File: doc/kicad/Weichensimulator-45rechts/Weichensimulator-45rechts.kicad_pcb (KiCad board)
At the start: 2 copper layers, 38.1 x 38.1 mm, 9 parts, among them J1 Conn_01x02_Male, J2 Power, J3 Conn_01x02_Male, K1 HFD2_005-S-L2-D

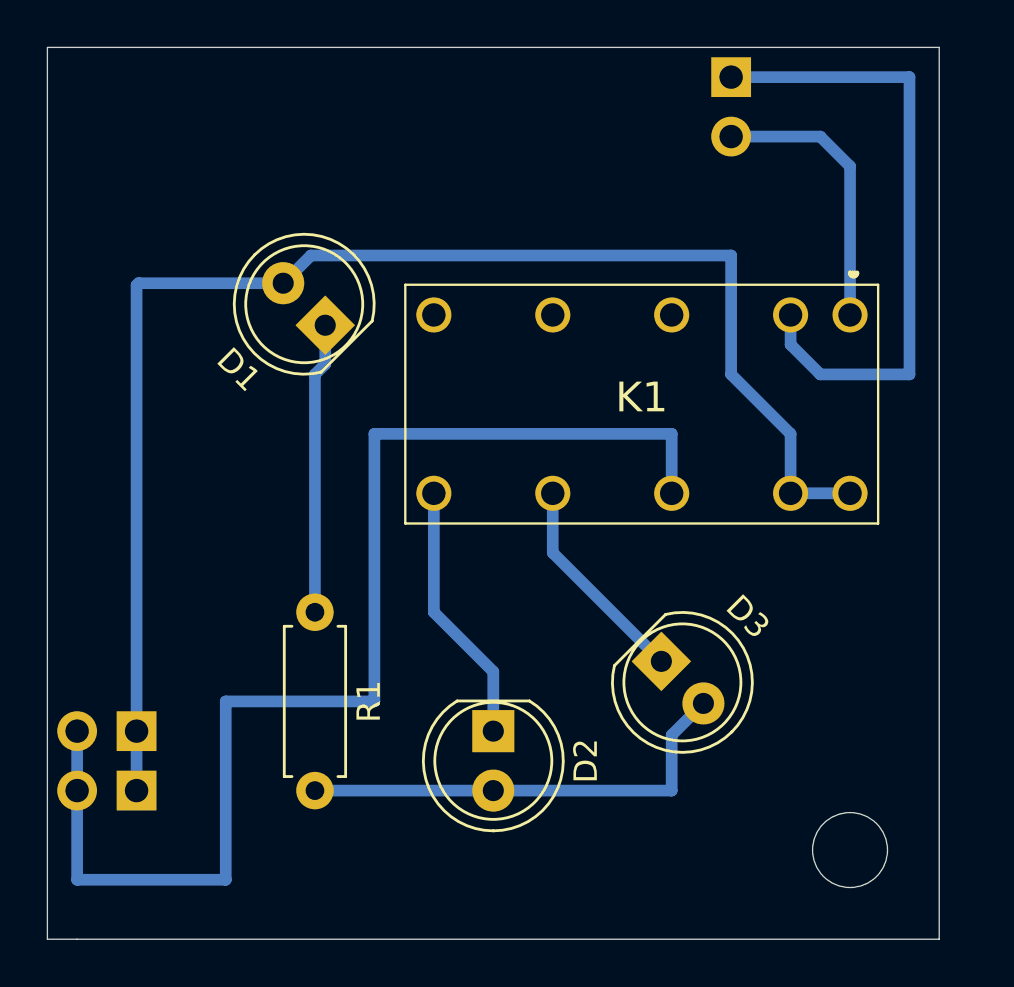
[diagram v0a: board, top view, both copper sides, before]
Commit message: Ecken rund gemacht, alle mit Montagelöcher
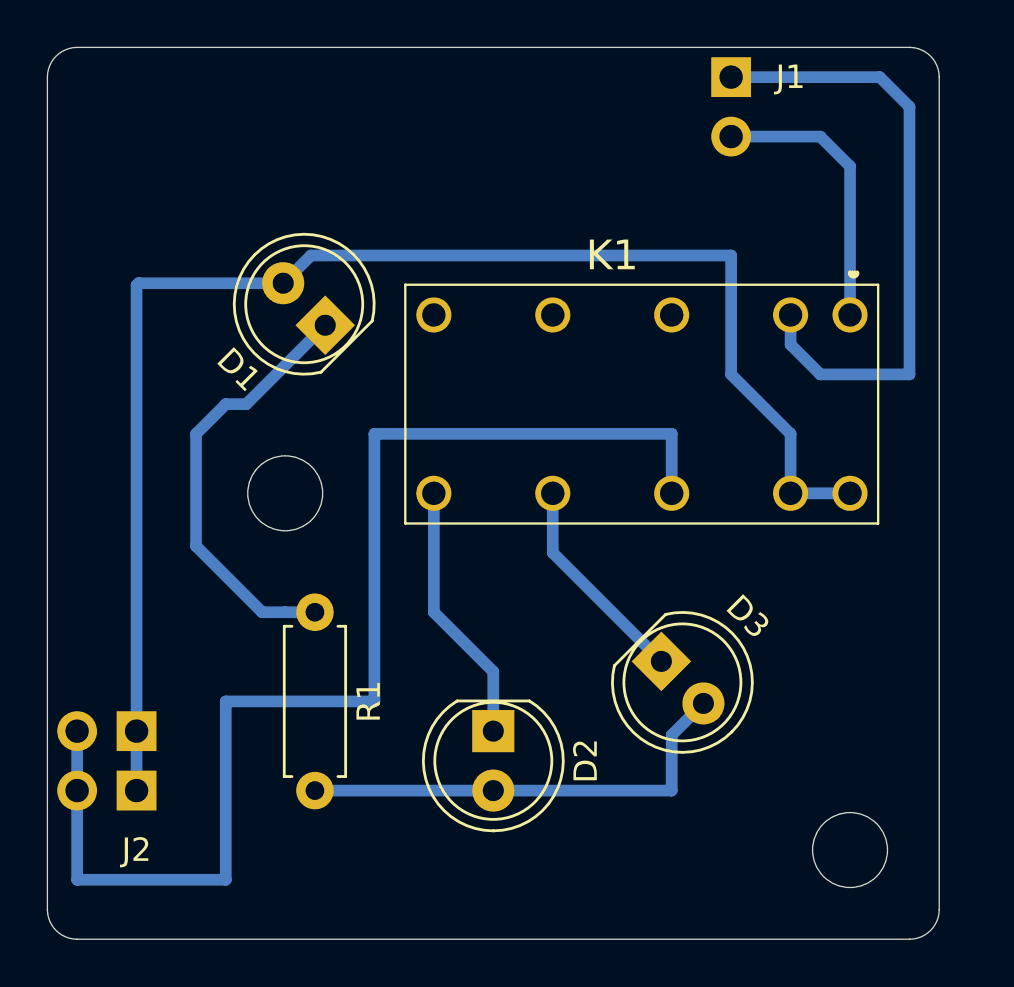
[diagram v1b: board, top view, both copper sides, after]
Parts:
- added H1: MountingHole, Mounting_Holes:MountingHole_3.2mm_M3, F.Cu at (139.7, 115.6)
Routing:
- net Net-(D1-Pad1): track 12.4 -> 18.5 mm
- net Net-(J1-Pad1): track 27.2 -> 26.5 mm
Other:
- outline, holes or cut-outs redrawn
- board text added: "©H3-H5N6 2021 Weiche re/45° v1.0"
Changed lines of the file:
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@@
-(kicad_pcb (version 20171130) (host pcbnew 5.1.9)
+(kicad_pcb (version 20171130) (host pcbnew 5.1.10)
   (general
     (thickness 1.6)
-    (drawings 5)
-    (tracks 38)
+    (drawings 9)
+    (tracks 43)
     (zones 0)
-    (modules 9)
+    (modules 10)
     (nets 9)
   )
@@
     (34 B.Paste user hide)
     (35 F.Paste user hide)
-    (36 B.SilkS user hide)
+    (36 B.SilkS user)
     (37 F.SilkS user)
     (38 B.Mask user)
@@
     (45 Margin user hide)
     (46 B.CrtYd user)
-    (47 F.CrtYd user hide)
+    (47 F.CrtYd user)
     (48 B.Fab user hide)
     (49 F.Fab user hide)
@@
     (add_net "Net-(J1-Pad2)")
   )
+  (module Mounting_Holes:MountingHole_3.2mm_M3 (layer F.Cu)
+    (at 139.7 115.57 270)
+    (descr "Mounting Hole 3.2mm, no annular, M3")
+    (tags "mounting hole 3.2mm no annular m3")
+    (attr virtual)
+    (fp_text reference H1 (at 0 -4.2 90) (layer F.SilkS) hide
+      (effects (font (size 1 1) (thickness 0.15)))
+    )
+    (fp_text value MountingHole (at 0 4.2 90) (layer F.Fab)
+      (effects (font (size 1 1) (thickness 0.15)))
+    )
+    (fp_text user %R (at 0.3 0 90) (layer F.Fab)
+      (effects (font (size 1 1) (thickness 0.15)))
+    )
+    (fp_circle (center 0 0) (end 3.2 0) (layer Cmts.User) (width 0.15))
+    (fp_circle (center 0 0) (end 3.45 0) (layer F.CrtYd) (width 0.05))
+    (pad "" np_thru_hole circle (at 0 0 270) (size 3.2 3.2) (drill 3.2) (layers *.Cu *.Mask)
+      (thermal_gap 2))
+  )
   (module LEDs:LED_D5.0mm (layer F.Cu)
     (at 141.41 108.39 135)
@@
     (descr HFD2/005-S-L2-D-3)
     (tags "Relay or Contactor")
-    (fp_text reference K1 (at 8.9 -3.53) (layer F.SilkS)
+    (fp_text reference K1 (at 10.16 2.54) (layer F.SilkS)
       (effects (font (size 1.27 1.27) (thickness 0.254)))
     )
@@
     (descr "Through hole angled pin header, 1x02, 2.54mm pitch, 6mm pin length, single row")
     (tags "Through hole angled pin header THT 1x02 2.54mm single row")
-    (fp_text reference J1 (at 4.385 2.27 180) (layer B.SilkS)
-      (effects (font (size 1 1) (thickness 0.15)) (justify mirror))
+    (fp_text reference J1 (at -2.54 0 180) (layer F.SilkS)
+      (effects (font (size 1 1) (thickness 0.15)))
     )
     (fp_text value Conn_01x02_Male (at 4.385 -4.81 180) (layer B.Fab)
@@
     (descr "Through hole angled pin header, 1x02, 2.54mm pitch, 6mm pin length, single row")
     (tags "Through hole angled pin header THT 1x02 2.54mm single row")
-    (fp_text reference J2 (at 4.385 2.27 90) (layer B.SilkS)
-      (effects (font (size 1 1) (thickness 0.15)) (justify mirror))
+    (fp_text reference J2 (at -5.08 0 180) (layer F.SilkS)
+      (effects (font (size 1 1) (thickness 0.15)))
     )
     (fp_text value Power (at 4.385 -4.81 90) (layer B.Fab)
@@
     (descr "Through hole angled pin header, 1x02, 2.54mm pitch, 6mm pin length, single row")
     (tags "Through hole angled pin header THT 1x02 2.54mm single row")
-    (fp_text reference J3 (at 4.385 2.27 90) (layer B.SilkS)
-      (effects (font (size 1 1) (thickness 0.15)) (justify mirror))
+    (fp_text reference J3 (at -2.54 0 180) (layer F.SilkS) hide
+      (effects (font (size 1 1) (thickness 0.15)))
     )
     (fp_text value Conn_01x02_Male (at 4.385 -4.81 90) (layer B.Fab)
@@
       (thermal_gap 2))
   )
-  (gr_line (start 129.54 134.62) (end 130.81 134.62) (layer Edge.Cuts) (width 0.05))
-  (gr_line (start 129.54 96.52) (end 167.64 96.52) (layer Edge.Cuts) (width 0.05))
-  (gr_line (start 129.54 134.62) (end 129.54 96.52) (layer Edge.Cuts) (width 0.05))
-  (gr_line (start 167.64 134.62) (end 130.81 134.62) (layer Edge.Cuts) (width 0.05))
-  (gr_line (start 167.64 96.52) (end 167.64 134.62) (layer Edge.Cuts) (width 0.05))
-  (segment (start 141.41 108.39) (end 141.41 110.05) (width 0.5) (layer B.Cu) (net 1))
-  (segment (start 141.41 110.05) (end 140.97 110.49) (width 0.5) (layer B.Cu) (net 1))
-  (segment (start 140.97 110.49) (end 140.97 120.65) (width 0.5) (layer B.Cu) (net 1))
+  (gr_text "©H3-H5N6 2021\nWeiche re/45° v1.0" (at 154.94 111.76) (layer B.SilkS)
+    (effects (font (size 1.5 1.5) (thickness 0.3)) (justify mirror))
+  )
+  (gr_arc (start 130.81 133.35) (end 129.54 133.35) (angle -90) (layer Edge.Cuts) (width 0.05))
+  (gr_arc (start 166.37 133.35) (end 166.37 134.62) (angle -90) (layer Edge.Cuts) (width 0.05))
+  (gr_arc (start 166.37 97.79) (end 167.64 97.79) (angle -90) (layer Edge.Cuts) (width 0.05))
+  (gr_arc (start 130.81 97.79) (end 130.81 96.52) (angle -90) (layer Edge.Cuts) (width 0.05))
+  (gr_line (start 130.81 96.52) (end 166.37 96.52) (layer Edge.Cuts) (width 0.05))
+  (gr_line (start 129.54 133.35) (end 129.54 97.79) (layer Edge.Cuts) (width 0.05))
+  (gr_line (start 166.37 134.62) (end 130.81 134.62) (layer Edge.Cuts) (width 0.05))
+  (gr_line (start 167.64 97.79) (end 167.64 133.35) (layer Edge.Cuts) (width 0.05))
+  (segment (start 139.7 120.65) (end 140.97 120.65) (width 0.5) (layer B.Cu) (net 1))
+  (segment (start 135.89 117.824001) (end 138.715999 120.65) (width 0.5) (layer B.Cu) (net 1))
+  (segment (start 138.715999 120.65) (end 139.7 120.65) (width 0.5) (layer B.Cu) (net 1))
+  (segment (start 135.89 113.03) (end 135.89 117.824001) (width 0.5) (layer B.Cu) (net 1))
+  (segment (start 137.16 111.76) (end 135.89 113.03) (width 0.5) (layer B.Cu) (net 1))
+  (segment (start 138.04 111.76) (end 137.16 111.76) (width 0.5) (layer B.Cu) (net 1))
+  (segment (start 141.41 108.39) (end 138.04 111.76) (width 0.5) (layer B.Cu) (net 1))
   (segment (start 146.05 115.57) (end 146.05 120.65) (width 0.5) (layer B.Cu) (net 2))
   (segment (start 146.05 120.65) (end 148.59 123.19) (width 0.5) (layer B.Cu) (net 2))
@@
   (segment (start 161.29 109.22) (end 162.56 110.49) (width 0.5) (layer B.Cu) (net 5))
   (segment (start 162.56 110.49) (end 166.37 110.49) (width 0.5) (layer B.Cu) (net 5))
-  (segment (start 166.37 110.49) (end 166.37 97.79) (width 0.5) (layer B.Cu) (net 5))
-  (segment (start 166.37 97.79) (end 158.75 97.79) (width 0.5) (layer B.Cu) (net 5))
+  (segment (start 166.37 99.06) (end 165.1 97.79) (width 0.5) (layer B.Cu) (net 5))
+  (segment (start 165.1 97.79) (end 158.75 97.79) (width 0.5) (layer B.Cu) (net 5))
+  (segment (start 166.37 99.06) (end 166.37 110.49) (width 0.5) (layer B.Cu) (net 5))
   (segment (start 133.35 125.73) (end 133.35 128.27) (width 0.5) (layer B.Cu) (net 6))
   (segment (start 139.613949 106.593949) (end 133.436051 106.593949) (width 0.5) (layer B.Cu) (net 6))

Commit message: Platinen, die an jlcpcb geschickt worden sind.
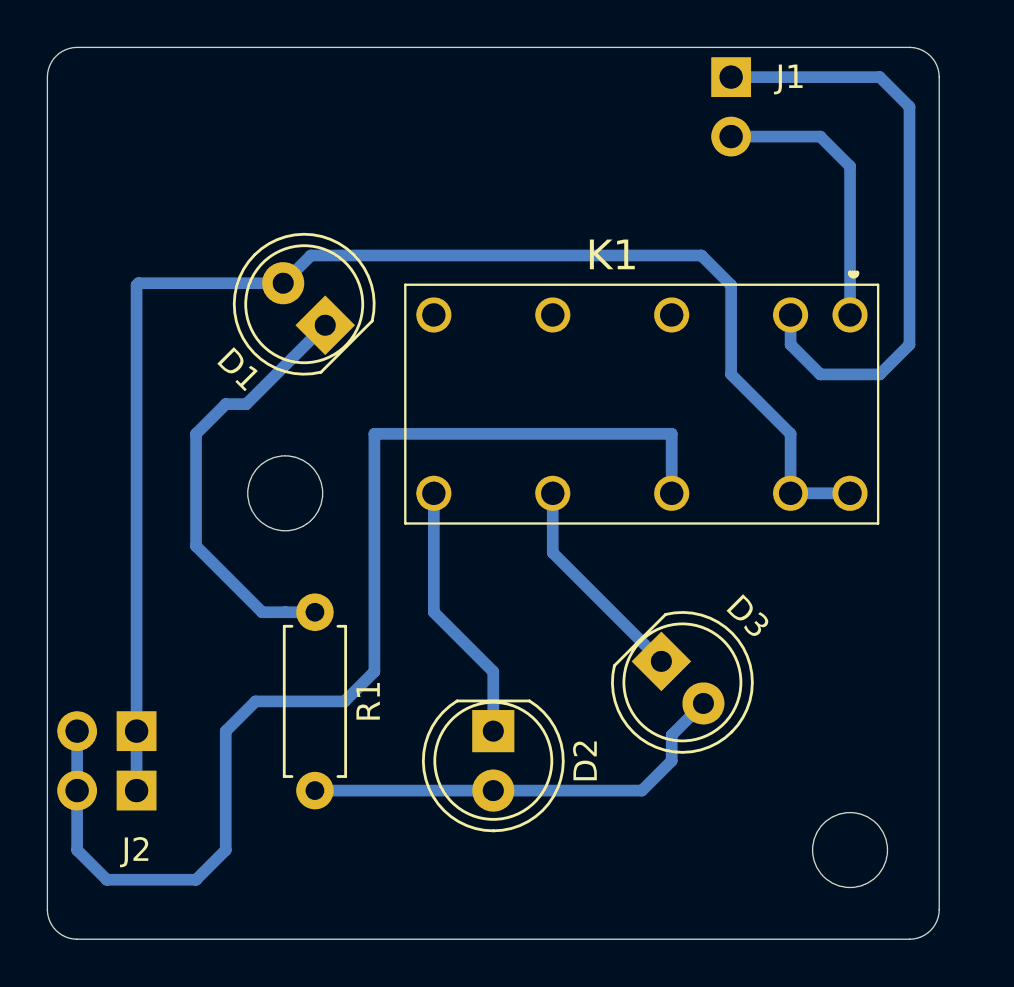
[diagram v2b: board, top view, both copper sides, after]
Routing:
- net GND: track 53.3 -> 50.4 mm
- net Net-(J1-Pad1): track 26.5 -> 25.7 mm
- net Net-(D2-Pad2): track 19.5 -> 18.8 mm
- net +5V: track 61.3 -> 60.5 mm
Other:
- board text added: "+5V"
- board text added: "A"
- board text added: "G"
- board text added: "GND"

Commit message: Bezeichnung nun auf der Besrückungsseite
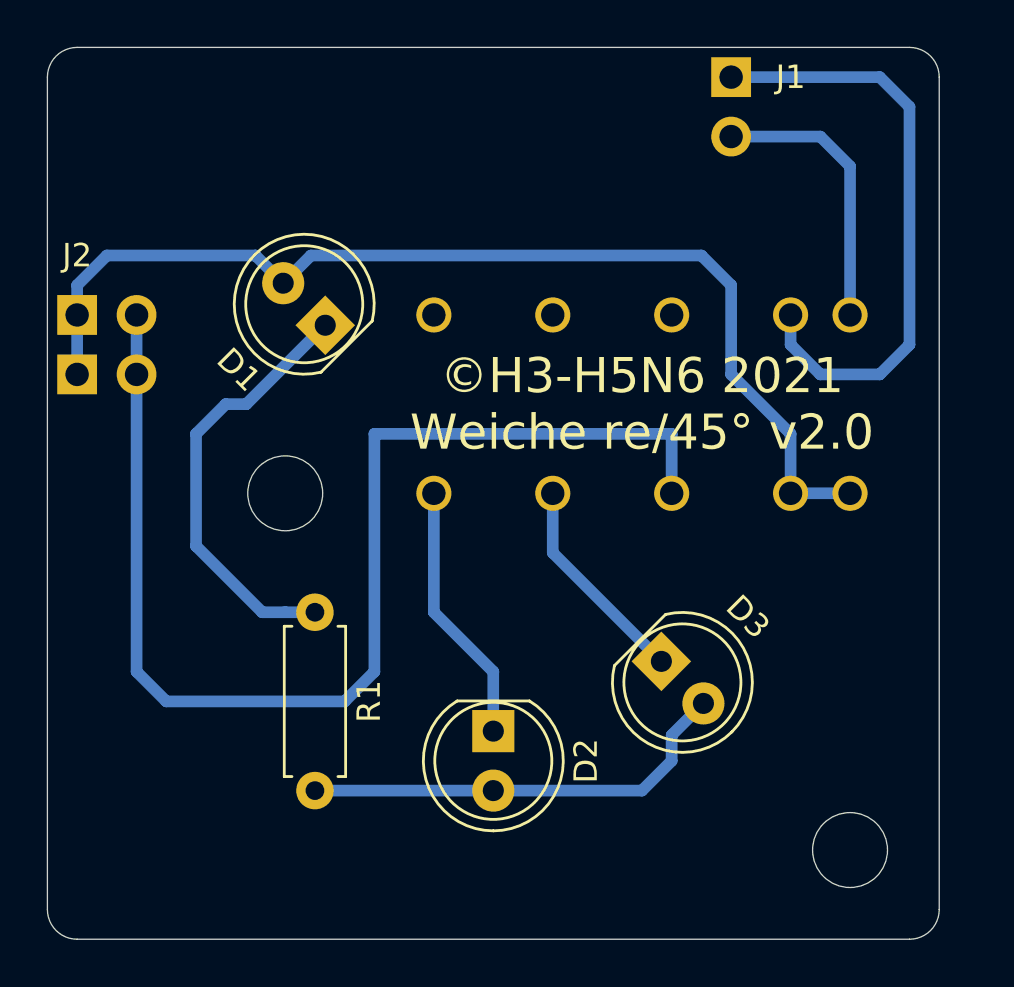
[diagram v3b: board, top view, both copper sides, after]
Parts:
- K1: moved to B.Cu
- moved J3 20.5 mm to (130.8, 108.0), turned to 270 degrees
- moved J2 15.5 mm to (130.8, 110.5), turned to 270 degrees
- moved K1 7.62 mm to (163.8, 115.6)
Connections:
- K1 pad 1: Net-(J1-Pad2) -> +5V
- K1 pad 11: Net-(D3-Pad1) -> (no net)
- K1 pad 13: GND -> (no net)
- K1 pad 15: +5V -> Net-(J1-Pad1)
- K1 pad 16: +5V -> Net-(J1-Pad2)
- K1 pad 2: Net-(J1-Pad1) -> +5V
- K1 pad 4: (no net) -> GND
- K1 pad 6: (no net) -> Net-(D3-Pad1)
- K1 pad 8: (no net) -> Net-(D2-Pad1)
- K1 pad 9: Net-(D2-Pad1) -> (no net)
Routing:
- net +5V: track 60.5 -> 46.3 mm
- net GND: track 50.4 -> 51.9 mm
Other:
- board text added: "©H3-H5N6 2021 Weiche re/45° v2.0"
- board text removed: "©H3-H5N6 2021 Weiche re/45° v1.0"

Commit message: Dateien aufgeräumt
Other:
- net class Default removed
